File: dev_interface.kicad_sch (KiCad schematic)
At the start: 21 parts, among them U10 ADS1014IDGS, U11 TLV9301xDBV, U12 DAC53401, U13 ADS1014IDGS, U9 ISO164xB

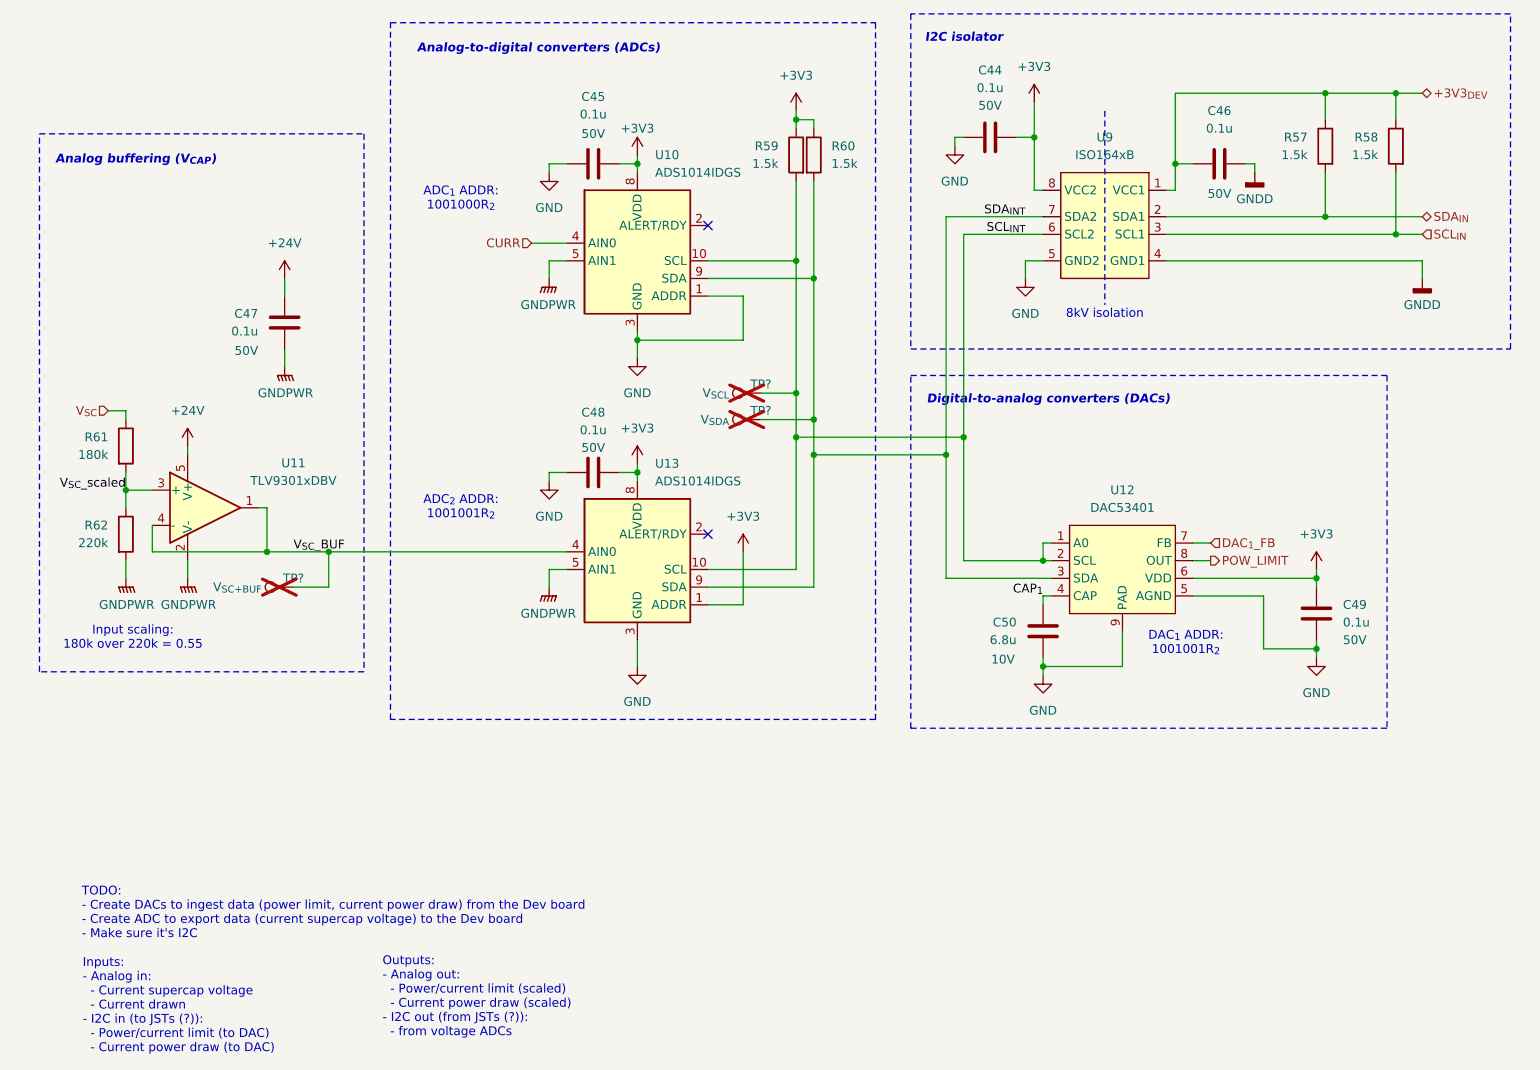
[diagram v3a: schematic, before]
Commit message: Replace most banana jacks with XT connectors
+ update library
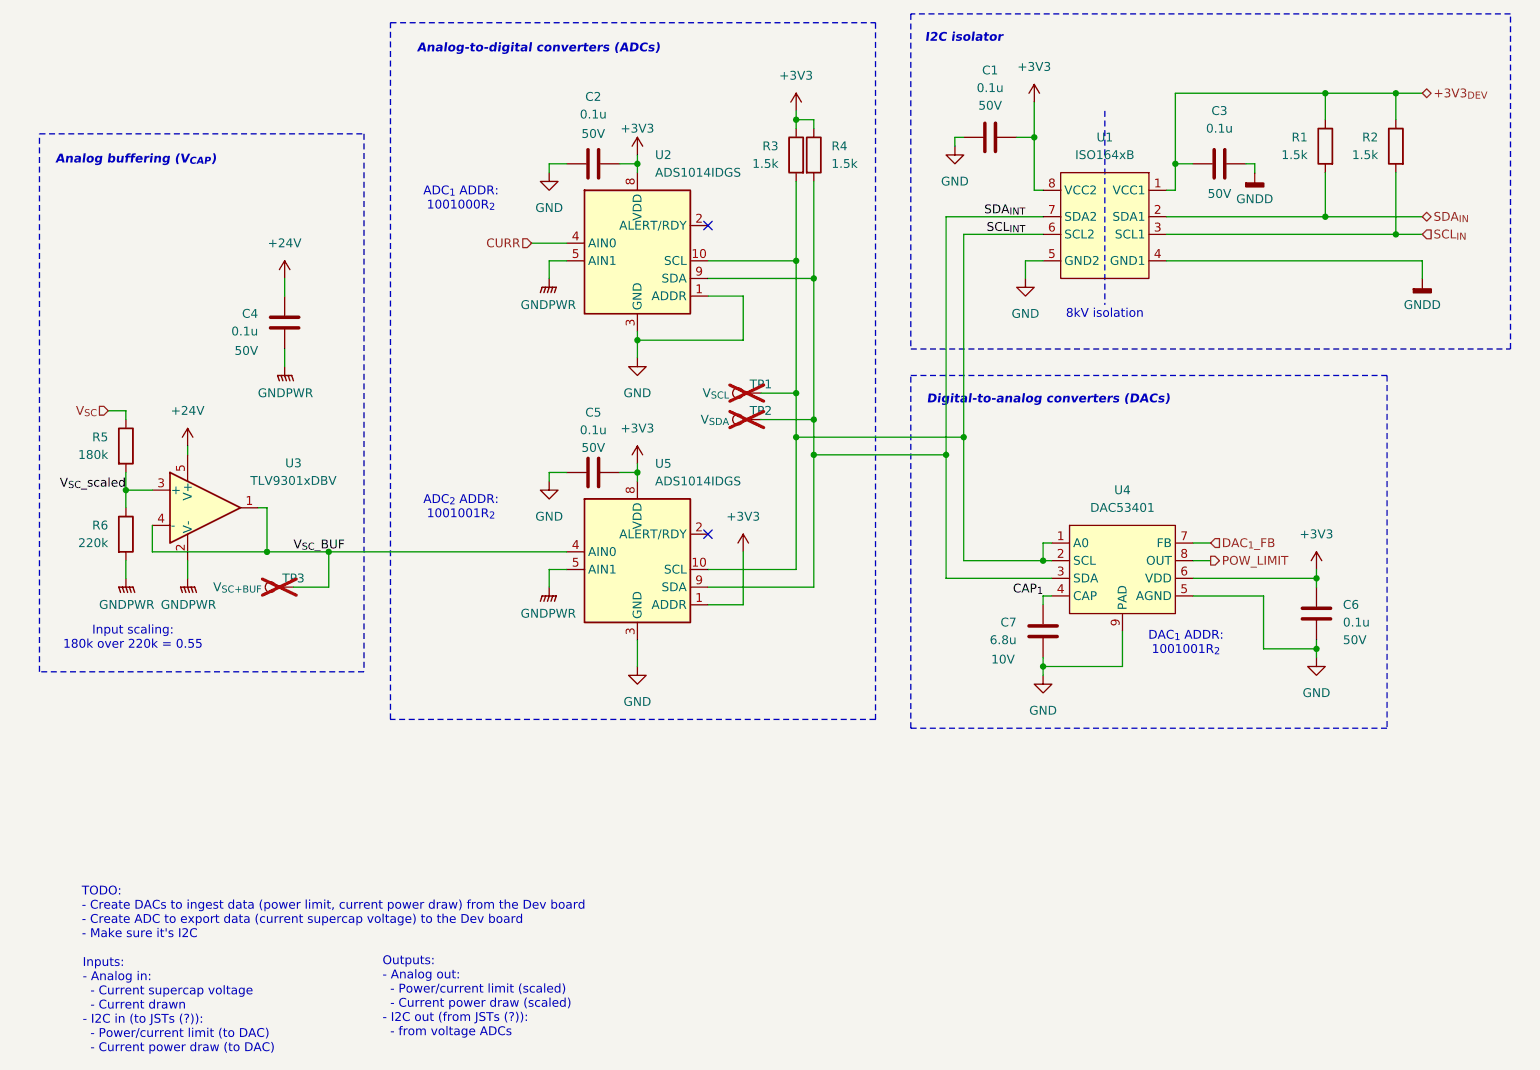
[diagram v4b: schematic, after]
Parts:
- gave numbers to parts that had none: 3
- renumbered C44 to C1, C45 to C2, C46 to C3, C47 to C4, C48 to C5, C49 to C6, C50 to C7, R57 to R1, R58 to R2, R59 to R3, R60 to R4, R61 to R5, R62 to R6, U9 to U1, U10 to U2, U11 to U3, U12 to U4, U13 to U5
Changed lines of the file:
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@@
 		(on_board yes)
 		(dnp no)
-		(property "Reference" "U13"
+		(property "Reference" "U5"
 			(at 132.08 104.14 0)
 			(effects
@@
 		(dnp no)
 		(fields_autoplaced yes)
-		(property "Reference" "#PWR067"
+		(property "Reference" "#PWR0101"
 			(at 185.42 83.82 0)
 			(effects
@@
 		(dnp no)
 		(fields_autoplaced yes)
-		(property "Reference" "#PWR081"
+		(property "Reference" "#PWR0110"
 			(at 129.54 139.7 0)
 			(effects
@@
 		(dnp no)
 		(fields_autoplaced yes)
-		(property "Reference" "#PWR069"
+		(property "Reference" "#PWR0122"
 			(at 129.54 95.25 0)
 			(effects
@@
 		(on_board yes)
 		(dnp yes)
-		(property "Reference" "TP?"
+		(property "Reference" "TP1"
 			(at 147.32 92.71 90)
 			(effects
@@
 		(on_board yes)
 		(dnp no)
-		(property "Reference" "C46"
+		(property "Reference" "C3"
 			(at 213.36 53.34 90)
 			(effects
@@
 		(dnp no)
 		(fields_autoplaced yes)
-		(property "Reference" "#PWR064"
+		(property "Reference" "#PWR0116"
 			(at 218.44 68.58 0)
 			(effects
@@
 		(dnp no)
 		(fields_autoplaced yes)
-		(property "Reference" "#PWR060"
+		(property "Reference" "#PWR0113"
 			(at 152.4 57.15 0)
 			(effects
@@
 		(dnp no)
 		(fields_autoplaced yes)
-		(property "Reference" "R59"
+		(property "Reference" "R3"
 			(at 149.86 58.4199 0)
 			(effects
@@
 		(dnp no)
 		(fields_autoplaced yes)
-		(property "Reference" "#PWR063"
+		(property "Reference" "#PWR0114"
 			(at 116.84 68.58 0)
 			(effects
@@
 		(on_board yes)
 		(dnp no)
-		(property "Reference" "#PWR062"
+		(property "Reference" "#PWR0115"
 			(at 129.54 63.5 0)
 			(effects
@@
 		(dnp no)
 		(fields_autoplaced yes)
-		(property "Reference" "U12"
+		(property "Reference" "U4"
 			(at 199.39 107.95 0)
 			(effects
@@
 		(on_board yes)
 		(dnp no)
-		(property "Reference" "C50"
+		(property "Reference" "C7"
 			(at 184.15 126.9999 0)
 			(effects
@@
 		(on_board yes)
 		(dnp no)
-		(property "Reference" "C47"
+		(property "Reference" "C4"
 			(at 74.93 82.5499 0)
 			(effects
@@
 		(on_board yes)
 		(dnp no)
-		(property "Reference" "C44"
+		(property "Reference" "C1"
 			(at 180.34 47.498 90)
 			(effects
@@
 		(dnp no)
 		(fields_autoplaced yes)
-		(property "Reference" "#PWR072"
+		(property "Reference" "#PWR0123"
 			(at 129.54 107.95 0)
 			(effects
@@
 		(on_board yes)
 		(dnp no)
-		(property "Reference" "U10"
+		(property "Reference" "U2"
 			(at 132.08 59.69 0)
 			(effects
@@
 		(dnp no)
 		(fields_autoplaced yes)
-		(property "Reference" "#PWR071"
+		(property "Reference" "#PWR0108"
 			(at 64.77 105.41 0)
 			(effects
@@
 		(on_board yes)
 		(dnp no)
-		(property "Reference" "R60"
+		(property "Reference" "R4"
 			(at 157.48 58.4199 0)
 			(effects
@@
 		(dnp no)
 		(fields_autoplaced yes)
-		(property "Reference" "#PWR070"
+		(property "Reference" "#PWR0107"
 			(at 78.74 95.25 0)
 			(effects
@@
 		(dnp no)
 		(fields_autoplaced yes)
-		(property "Reference" "#PWR075"
+		(property "Reference" "#PWR0121"
 			(at 144.78 120.65 0)
 			(effects
@@
 		(dnp no)
 		(fields_autoplaced yes)
-		(property "Reference" "#PWR065"
+		(property "Reference" "#PWR0104"
 			(at 78.74 81.28 0)
 			(effects
@@
 		(on_board yes)
 		(dnp yes)
-		(property "Reference" "TP?"
+		(property "Reference" "TP2"
 			(at 147.32 96.52 90)
 			(effects
@@
 		(dnp no)
 		(fields_autoplaced yes)
-		(property "Reference" "#PWR077"
+		(property "Reference" "#PWR0120"
 			(at 227.33 123.19 0)
 			(effects
@@
 		(dnp no)
 		(fields_autoplaced yes)
-		(property "Reference" "#PWR082"
+		(property "Reference" "#PWR0118"
 			(at 187.96 140.97 0)
 			(effects
@@
 		(dnp no)
 		(fields_autoplaced yes)
-		(property "Reference" "U11"
+		(property "Reference" "U3"
 			(at 80.01 104.0698 0)
 			(effects
@@
 		(on_board yes)
 		(dnp no)
-		(property "Reference" "C48"
+		(property "Reference" "C5"
 			(at 123.19 96.774 90)
 			(effects
@@
 		(dnp no)
 		(fields_autoplaced yes)
-		(property "Reference" "#PWR061"
+		(property "Reference" "#PWR0102"
 			(at 175.26 64.77 0)
 			(effects
@@
 		(dnp no)
 		(fields_autoplaced yes)
-		(property "Reference" "R57"
+		(property "Reference" "R1"
 			(at 226.06 57.1499 0)
 			(effects
@@
 		(on_board yes)
 		(dnp no)
-		(property "Reference" "R62"
+		(property "Reference" "R6"
 			(at 53.34 113.0299 0)
 			(effects
@@
 		(on_board yes)
 		(dnp no)
-		(property "Reference" "R61"
+		(property "Reference" "R5"
 			(at 53.34 100.3299 0)
 			(effects
@@
 		(dnp no)
 		(fields_autoplaced yes)
-		(property "Reference" "#PWR059"
+		(property "Reference" "#PWR0103"
 			(at 186.69 55.88 0)
 			(effects
@@
 		(on_board yes)
 		(dnp no)
-		(property "Reference" "U9"
+		(property "Reference" "U1"
 			(at 196.85 57.15 0)
 			(effects
@@
 		(dnp no)
 		(fields_autoplaced yes)
-		(property "Reference" "#PWR073"
+		(property "Reference" "#PWR0111"
 			(at 116.84 113.03 0)
 			(effects
@@
 		(dnp no)
 		(fields_autoplaced yes)
-		(property "Reference" "#PWR?"
+		(property "Reference" "#PWR0105"
 			(at 55.88 125.73 0)
 			(effects
@@
 		(on_board yes)
 		(dnp yes)
-		(property "Reference" "TP?"
+		(property "Reference" "TP3"
 			(at 80.01 120.65 90)
 			(effects
@@
 		(dnp no)
 		(fields_autoplaced yes)
-		(property "Reference" "#PWR080"
+		(property "Reference" "#PWR0119"
 			(at 227.33 138.43 0)
 			(effects
@@
 		(dnp no)
 		(fields_autoplaced yes)
-		(property "Reference" "#PWR068"
+		(property "Reference" "#PWR0117"
 			(at 242.57 83.82 0)
 			(effects
@@
 		(dnp no)
 		(fields_autoplaced yes)
-		(property "Reference" "#PWR066"
+		(property "Reference" "#PWR0109"
 			(at 116.84 82.55 0)
 			(effects
@@
 		(on_board yes)
 		(dnp no)
-		(property "Reference" "C49"
+		(property "Reference" "C6"
 			(at 231.14 124.4599 0)
 			(effects
@@
 		(on_board yes)
 		(dnp no)
-		(property "Reference" "C45"
+		(property "Reference" "C2"
 			(at 123.19 51.308 90)
 			(effects
@@
 		(dnp no)
 		(fields_autoplaced yes)
-		(property "Reference" "R58"
+		(property "Reference" "R2"
 			(at 236.22 57.1499 0)
 			(effects
@@
 		(dnp no)
 		(fields_autoplaced yes)
-		(property "Reference" "#PWR078"
+		(property "Reference" "#PWR0106"
 			(at 64.77 125.73 0)
 			(effects
@@
 		(dnp no)
 		(fields_autoplaced yes)
-		(property "Reference" "#PWR079"
+		(property "Reference" "#PWR0112"
 			(at 116.84 127 0)
 			(effects
